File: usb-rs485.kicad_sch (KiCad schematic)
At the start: 14 parts, among them M1 THRU_HOLE_PAD, M2 THRU_HOLE_PAD

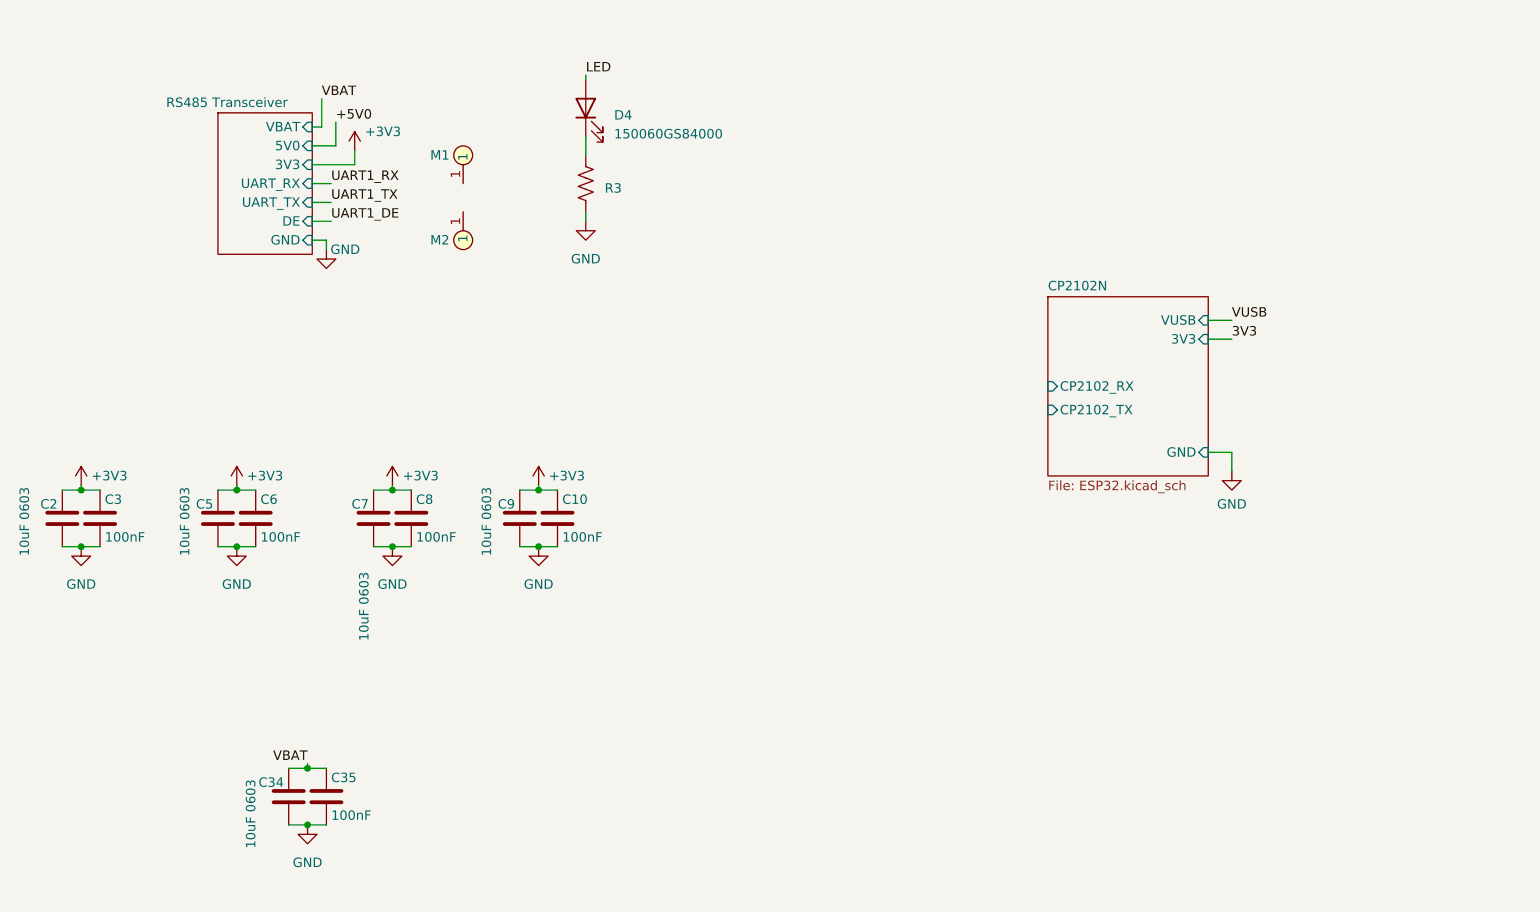
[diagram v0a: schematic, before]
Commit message: gitignore, datasheet for cp2102n added
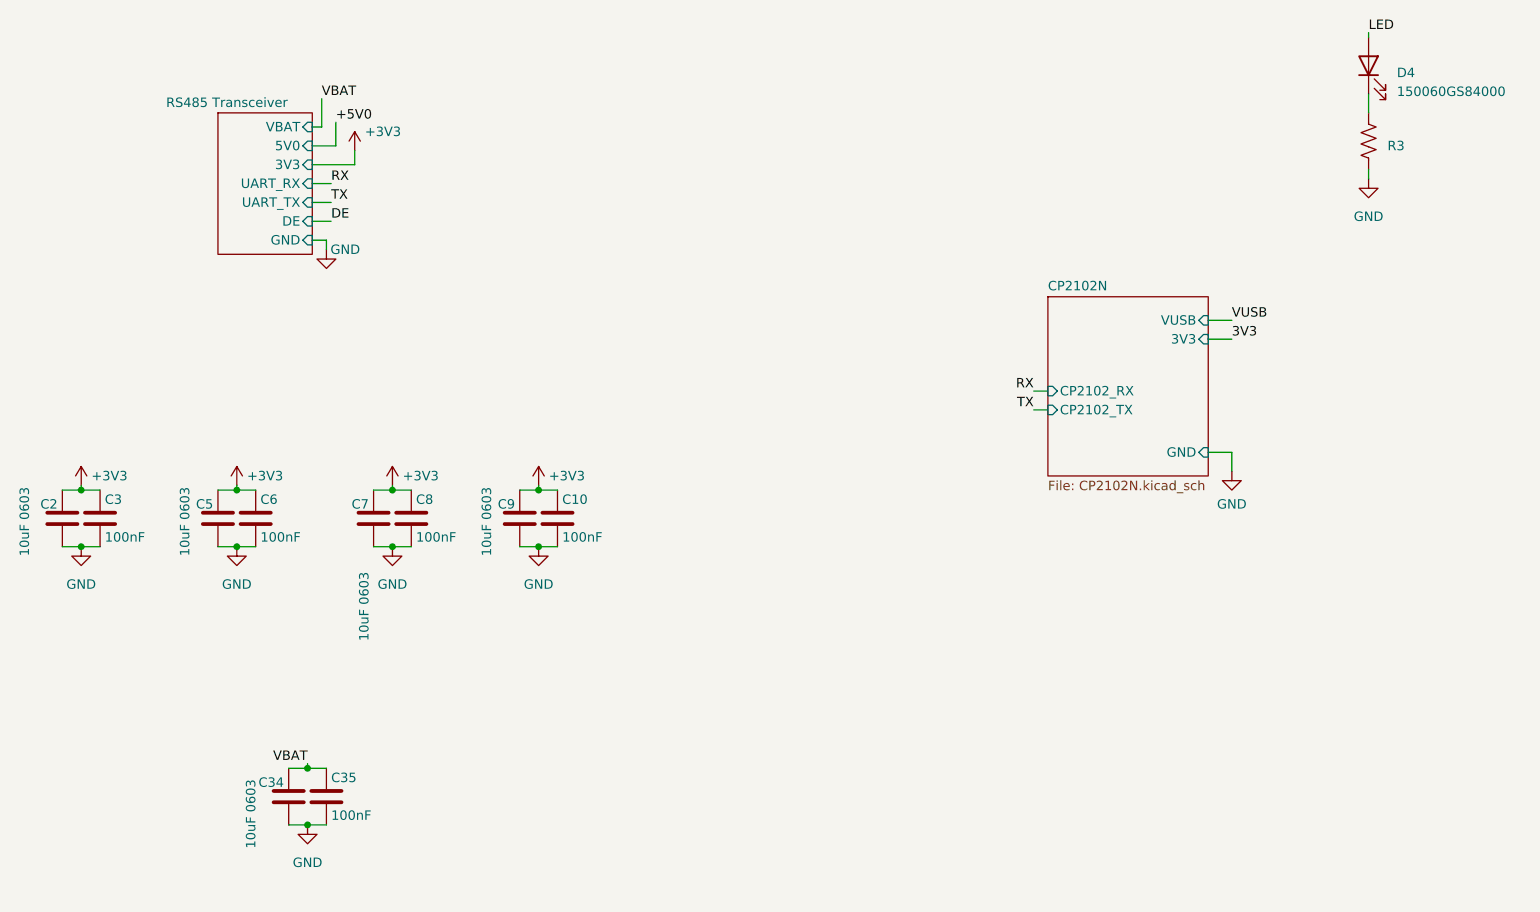
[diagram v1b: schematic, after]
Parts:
- removed M1, M2: THRU_HOLE_PAD, robot-cortex:TEARDROP, symbol foc-pcb:THRU_HOLE_PAD
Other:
- sheet CP2102N: file ESP32.kicad_sch -> CP2102N.kicad_sch
- moved on the sheet: D4, R3
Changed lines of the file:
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@@
     (stroke (width 0) (type default))
   )
-  (wire (pts (xy 229.235 116.205) (xy 229.235 118.745))
+  (wire (pts (xy 334.645 110.49) (xy 334.645 113.03))
     (stroke (width 0) (type default))
   )
@@
     (stroke (width 0) (type default))
   )
-  (wire (pts (xy 229.235 127.635) (xy 229.235 126.365))
+  (wire (pts (xy 334.645 121.92) (xy 334.645 120.65))
     (stroke (width 0) (type default))
   )
@@
     (stroke (width 0) (type default))
   )
+  (wire (pts (xy 289.56 150.495) (xy 291.465 150.495))
+    (stroke (width 0) (type default))
+  )
   (wire (pts (xy 193.675 111.125) (xy 193.675 114.935))
     (stroke (width 0) (type default))
@@
     (stroke (width 0) (type default))
   )
-  (wire (pts (xy 229.235 107.95) (xy 229.235 108.585))
+  (wire (pts (xy 334.645 102.235) (xy 334.645 102.87))
     (stroke (width 0) (type default))
   )
   (wire (pts (xy 225.425 171.45) (xy 222.885 171.45))
+    (stroke (width 0) (type default))
+  )
+  (wire (pts (xy 289.56 153.035) (xy 291.465 153.035))
     (stroke (width 0) (type default))
   )
@@
     (effects (font (size 1.27 1.27)) (justify left bottom))
   )
-  (label "UART1_TX" (at 194.945 125.095 0) (fields_autoplaced)
+  (label "TX" (at 194.945 125.095 0) (fields_autoplaced)
     (effects (font (size 1.27 1.27)) (justify left bottom))
   )
-  (label "UART1_DE" (at 194.945 127.635 0) (fields_autoplaced)
+  (label "DE" (at 194.945 127.635 0) (fields_autoplaced)
     (effects (font (size 1.27 1.27)) (justify left bottom))
   )
@@
     (effects (font (size 1.27 1.27)) (justify left bottom))
   )
-  (label "UART1_RX" (at 194.945 122.555 0) (fields_autoplaced)
+  (label "RX" (at 194.945 122.555 0) (fields_autoplaced)
     (effects (font (size 1.27 1.27)) (justify left bottom))
   )
@@
     (effects (font (size 1.27 1.27)) (justify left bottom))
   )
-  (label "LED" (at 229.235 107.95 0) (fields_autoplaced)
+  (label "LED" (at 334.645 102.235 0) (fields_autoplaced)
     (effects (font (size 1.27 1.27)) (justify left bottom))
   )
   (label "3V3" (at 316.23 143.51 0) (fields_autoplaced)
     (effects (font (size 1.27 1.27)) (justify left bottom))
+  )
+  (label "TX" (at 289.56 153.035 180) (fields_autoplaced)
+    (effects (font (size 1.27 1.27)) (justify right bottom))
+  )
+  (label "RX" (at 289.56 150.495 180) (fields_autoplaced)
+    (effects (font (size 1.27 1.27)) (justify right bottom))
   )
   (symbol (lib_id "power:GND") (at 194.31 131.445 0) (mirror y) (unit 1)
@@
     )
   )
-  (symbol (lib_id "power:GND") (at 229.235 127.635 0) (mirror y) (unit 1)
+  (symbol (lib_id "power:GND") (at 334.645 121.92 0) (mirror y) (unit 1)
     (in_bom yes) (on_board yes) (dnp no) (fields_autoplaced)
-    (property "Reference" "#PWR03" (at 229.235 133.985 0)
-      (effects (font (size 1.27 1.27)) hide)
-    )
-    (property "Value" "GND" (at 229.235 132.715 0)
-      (effects (font (size 1.27 1.27)))
-    )
-    (property "Footprint" "" (at 229.235 127.635 0)
-      (effects (font (size 1.27 1.27)) hide)
-    )
-    (property "Datasheet" "" (at 229.235 127.635 0)
+    (property "Reference" "#PWR03" (at 334.645 128.27 0)
+      (effects (font (size 1.27 1.27)) hide)
+    )
+    (property "Value" "GND" (at 334.645 127 0)
+      (effects (font (size 1.27 1.27)))
+    )
+    (property "Footprint" "" (at 334.645 121.92 0)
+      (effects (font (size 1.27 1.27)) hide)
+    )
+    (property "Datasheet" "" (at 334.645 121.92 0)
       (effects (font (size 1.27 1.27)) hide)
     )
@@
     )
   )
-  (symbol (lib_id "foc-pcb:Resistor") (at 229.235 122.555 0) (unit 1)
+  (symbol (lib_id "foc-pcb:Resistor") (at 334.645 116.84 0) (unit 1)
     (in_bom yes) (on_board yes) (dnp no) (fields_autoplaced)
-    (property "Reference" "R3" (at 231.775 123.19 0)
-      (effects (font (size 1.27 1.27)) (justify left))
-    )
-    (property "Value" "470" (at 226.695 122.555 90)
-      (effects (font (size 1.27 1.27)) hide)
-    )
-    (property "Footprint" "robot-cortex:R_0402_1005Metric" (at 224.155 109.855 0)
-      (effects (font (size 1.27 1.27)) hide)
-    )
-    (property "Datasheet" "~" (at 229.235 122.555 0)
+    (property "Reference" "R3" (at 337.185 117.475 0)
+      (effects (font (size 1.27 1.27)) (justify left))
+    )
+    (property "Value" "470" (at 332.105 116.84 90)
+      (effects (font (size 1.27 1.27)) hide)
+    )
+    (property "Footprint" "robot-cortex:R_0402_1005Metric" (at 329.565 104.14 0)
+      (effects (font (size 1.27 1.27)) hide)
+    )
+    (property "Datasheet" "~" (at 334.645 116.84 0)
       (effects (font (size 1.27 1.27)) hide)
     )
@@
     )
   )
-  (symbol (lib_id "foc-pcb:THRU_HOLE_PAD") (at 212.725 128.905 270) (unit 1)
-    (in_bom no) (on_board yes) (dnp no)
-    (property "Reference" "M2" (at 208.28 130.175 90)
-      (effects (font (size 1.27 1.27)) (justify left))
-    )
-    (property "Value" "THRU_HOLE_PAD" (at 216.535 128.905 0)
-      (effects (font (size 1.27 1.27)) hide)
-    )
-    (property "Footprint" "robot-cortex:TEARDROP" (at 215.265 131.445 0)
-      (effects (font (size 1.27 1.27)) hide)
-    )
-    (property "Datasheet" "" (at 212.725 128.905 0)
-      (effects (font (size 1.27 1.27)) hide)
-    )
-    (pin "1")
-    (instances
-      (project "usb-rs485"
-        (path "/19e4cb9f-d0a4-4ce0-8aa4-5fe95563dc37"
-          (reference "M2") (unit 1)
-        )
-      )
-      (project "foc-pcb"
-        (path "/2b52ab19-a93e-4439-8602-a1380e4825c0"
-          (reference "M1") (unit 1)
-        )
-      )
-    )
-  )
-  (symbol (lib_id "foc-pcb:LED") (at 229.235 112.395 90) (unit 1)
+  (symbol (lib_id "foc-pcb:LED") (at 334.645 106.68 90) (unit 1)
     (in_bom yes) (on_board yes) (dnp no) (fields_autoplaced)
-    (property "Reference" "D4" (at 233.045 113.3475 90)
-      (effects (font (size 1.27 1.27)) (justify right))
-    )
-    (property "Value" "150060GS84000" (at 233.045 115.8875 90)
-      (effects (font (size 1.27 1.27)) (justify right))
-    )
-    (property "Footprint" "robot-cortex:LED_0603_1608Metric" (at 229.235 112.395 0)
-      (effects (font (size 1.27 1.27)) hide)
-    )
-    (property "Datasheet" "https://www.we-online.com/components/products/datasheet/150060GS84000.pdf" (at 229.235 112.395 0)
+    (property "Reference" "D4" (at 338.455 107.6325 90)
+      (effects (font (size 1.27 1.27)) (justify right))
+    )
+    (property "Value" "150060GS84000" (at 338.455 110.1725 90)
+      (effects (font (size 1.27 1.27)) (justify right))
+    )
+    (property "Footprint" "robot-cortex:LED_0603_1608Metric" (at 334.645 106.68 0)
+      (effects (font (size 1.27 1.27)) hide)
+    )
+    (property "Datasheet" "https://www.we-online.com/components/products/datasheet/150060GS84000.pdf" (at 334.645 106.68 0)
       (effects (font (size 1.27 1.27)) hide)
     )
@@
         (path "/2b52ab19-a93e-4439-8602-a1380e4825c0"
           (reference "C10") (unit 1)
-        )
-      )
-    )
-  )
-  (symbol (lib_id "foc-pcb:THRU_HOLE_PAD") (at 212.725 120.015 90) (unit 1)
-    (in_bom no) (on_board yes) (dnp no)
-    (property "Reference" "M1" (at 208.28 118.745 90)
-      (effects (font (size 1.27 1.27)) (justify right))
-    )
-    (property "Value" "THRU_HOLE_PAD" (at 208.915 120.015 0)
-      (effects (font (size 1.27 1.27)) hide)
-    )
-    (property "Footprint" "robot-cortex:TEARDROP" (at 210.185 117.475 0)
-      (effects (font (size 1.27 1.27)) hide)
-    )
-    (property "Datasheet" "" (at 212.725 120.015 0)
-      (effects (font (size 1.27 1.27)) hide)
-    )
-    (pin "1")
-    (instances
-      (project "usb-rs485"
-        (path "/19e4cb9f-d0a4-4ce0-8aa4-5fe95563dc37"
-          (reference "M1") (unit 1)
-        )
-      )
-      (project "foc-pcb"
-        (path "/2b52ab19-a93e-4439-8602-a1380e4825c0"
-          (reference "M1") (unit 1)
         )
       )
@@
       (effects (font (size 1.27 1.27)) (justify left bottom))
     )
-    (property "Sheetfile" "ESP32.kicad_sch" (at 291.465 162.5096 0)
+    (property "Sheetfile" "CP2102N.kicad_sch" (at 291.465 162.5096 0)
       (effects (font (size 1.27 1.27)) (justify left top))
     )
@@
       (effects (font (size 1.27 1.27)) (justify right))
     )
-    (pin "CP2102_RX" input (at 291.465 149.86 180)
-      (effects (font (size 1.27 1.27)) (justify left))
-    )
+    (pin "CP2102_RX" input (at 291.465 150.495 180)
+      (effects (font (size 1.27 1.27)) (justify left))
+    )

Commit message: backups removalled schematic looking correct if not good
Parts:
- removed C34: 10uF 0603, robot-cortex:C_0603_1608Metric, symbol foc-pcb:Capacitor
- removed C35: 100nF, robot-cortex:C_0402_1005Metric, symbol foc-pcb:Capacitor
- removed D4: 150060GS84000, robot-cortex:LED_0603_1608Metric, symbol foc-pcb:LED
- removed R3: 470, robot-cortex:R_0402_1005Metric, symbol foc-pcb:Resistor
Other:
- sheet CP2102N ports: added RS485; removed none
- sheet RS485 Transceiver ports: added none; removed VBAT

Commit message: library table
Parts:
- C10, C2, C3, C5, C6, C7, C8, C9: symbol foc-pcb:Capacitor -> usb-rs485:Capacitor
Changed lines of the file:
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@@
     )
   )
-  (symbol (lib_id "foc-pcb:Capacitor") (at 158.75 167.64 0) (mirror y) (unit 1)
+  (symbol (lib_id "usb-rs485:Capacitor") (at 158.75 167.64 0) (mirror y) (unit 1)
     (in_bom yes) (on_board yes) (dnp no)
     (property "Reference" "C2" (at 158.115 165.735 0)
@@
     )
   )
-  (symbol (lib_id "foc-pcb:Capacitor") (at 179.705 167.64 0) (mirror y) (unit 1)
+  (symbol (lib_id "usb-rs485:Capacitor") (at 179.705 167.64 0) (mirror y) (unit 1)
     (in_bom yes) (on_board yes) (dnp no)
     (property "Reference" "C5" (at 179.07 165.735 0)
@@
     )
   )
-  (symbol (lib_id "foc-pcb:Capacitor") (at 225.425 167.64 0) (unit 1)
+  (symbol (lib_id "usb-rs485:Capacitor") (at 225.425 167.64 0) (unit 1)
     (in_bom yes) (on_board yes) (dnp no)
     (property "Reference" "C10" (at 226.06 165.1 0)
@@
     )
   )
-  (symbol (lib_id "foc-pcb:Capacitor") (at 220.345 167.64 0) (mirror y) (unit 1)
+  (symbol (lib_id "usb-rs485:Capacitor") (at 220.345 167.64 0) (mirror y) (unit 1)
     (in_bom yes) (on_board yes) (dnp no)
     (property "Reference" "C9" (at 219.71 165.735 0)
@@
     )
   )
-  (symbol (lib_id "foc-pcb:Capacitor") (at 184.785 167.64 0) (unit 1)
+  (symbol (lib_id "usb-rs485:Capacitor") (at 184.785 167.64 0) (unit 1)
     (in_bom yes) (on_board yes) (dnp no)
     (property "Reference" "C6" (at 185.42 165.1 0)
@@
     )
   )
-  (symbol (lib_id "foc-pcb:Capacitor") (at 163.83 167.64 0) (unit 1)
+  (symbol (lib_id "usb-rs485:Capacitor") (at 163.83 167.64 0) (unit 1)
     (in_bom yes) (on_board yes) (dnp no)
     (property "Reference" "C3" (at 164.465 165.1 0)
@@
     )
   )
-  (symbol (lib_id "foc-pcb:Capacitor") (at 205.74 167.64 0) (unit 1)
+  (symbol (lib_id "usb-rs485:Capacitor") (at 205.74 167.64 0) (unit 1)
     (in_bom yes) (on_board yes) (dnp no)
     (property "Reference" "C8" (at 206.375 165.1 0)
@@
     )
   )
-  (symbol (lib_id "foc-pcb:Capacitor") (at 200.66 167.64 0) (mirror y) (unit 1)
+  (symbol (lib_id "usb-rs485:Capacitor") (at 200.66 167.64 0) (mirror y) (unit 1)
     (in_bom yes) (on_board yes) (dnp no)
     (property "Reference" "C7" (at 200.025 165.735 0)

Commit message: routing
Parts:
- removed C10, C3, C6, C8: 100nF, robot-cortex:C_0402_1005Metric, symbol usb-rs485:Capacitor
- removed C2, C5, C7, C9: 10uF 0603, robot-cortex:C_0603_1608Metric, symbol usb-rs485:Capacitor
